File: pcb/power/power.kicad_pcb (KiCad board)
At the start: 2 copper layers, 114.3 x 74.9 mm, 27 parts, among them K1 CONN_3, P1 CONN_3X2, P2 CONN_3X2, T1 TRANSFORMER_F24-800-C2, U1 MC34063

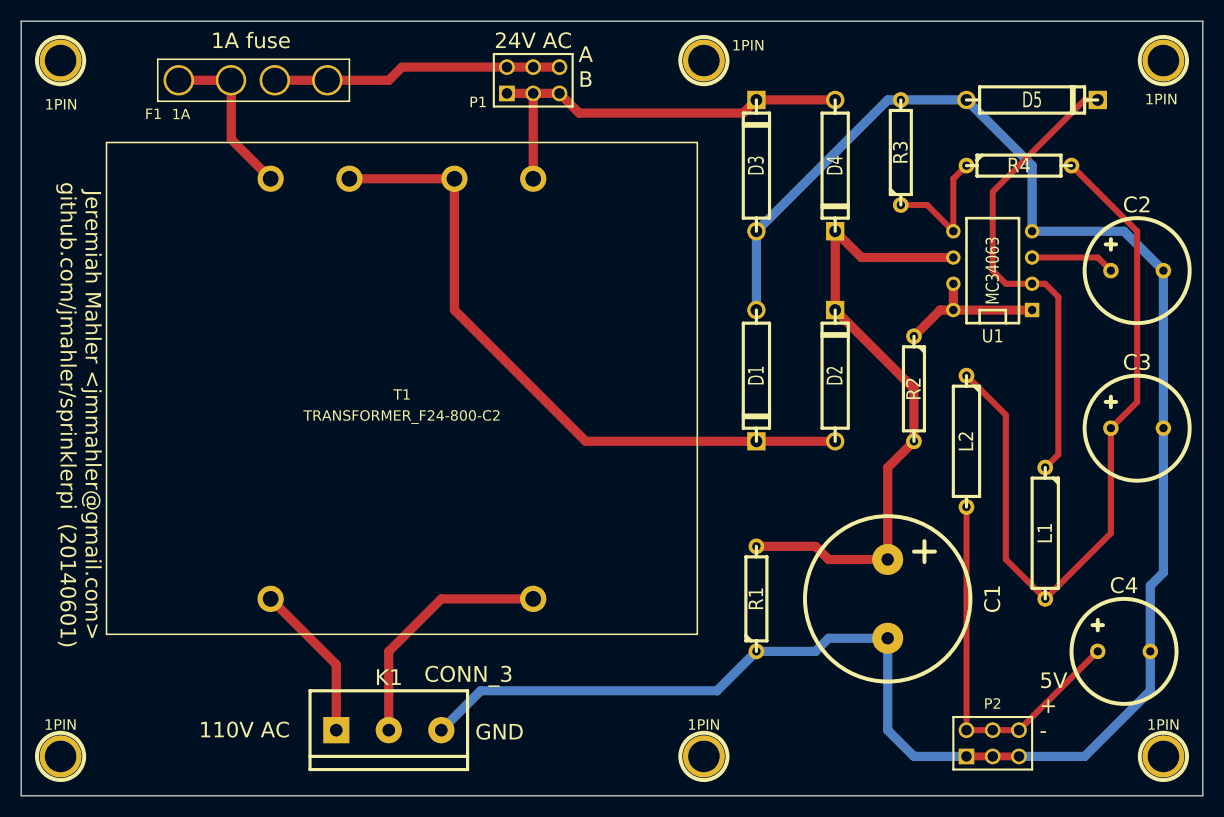
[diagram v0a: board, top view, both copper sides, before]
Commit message: proper size toroid inductor for power PCB
The power PCB has been changed to support
the proper size toroid inductor.
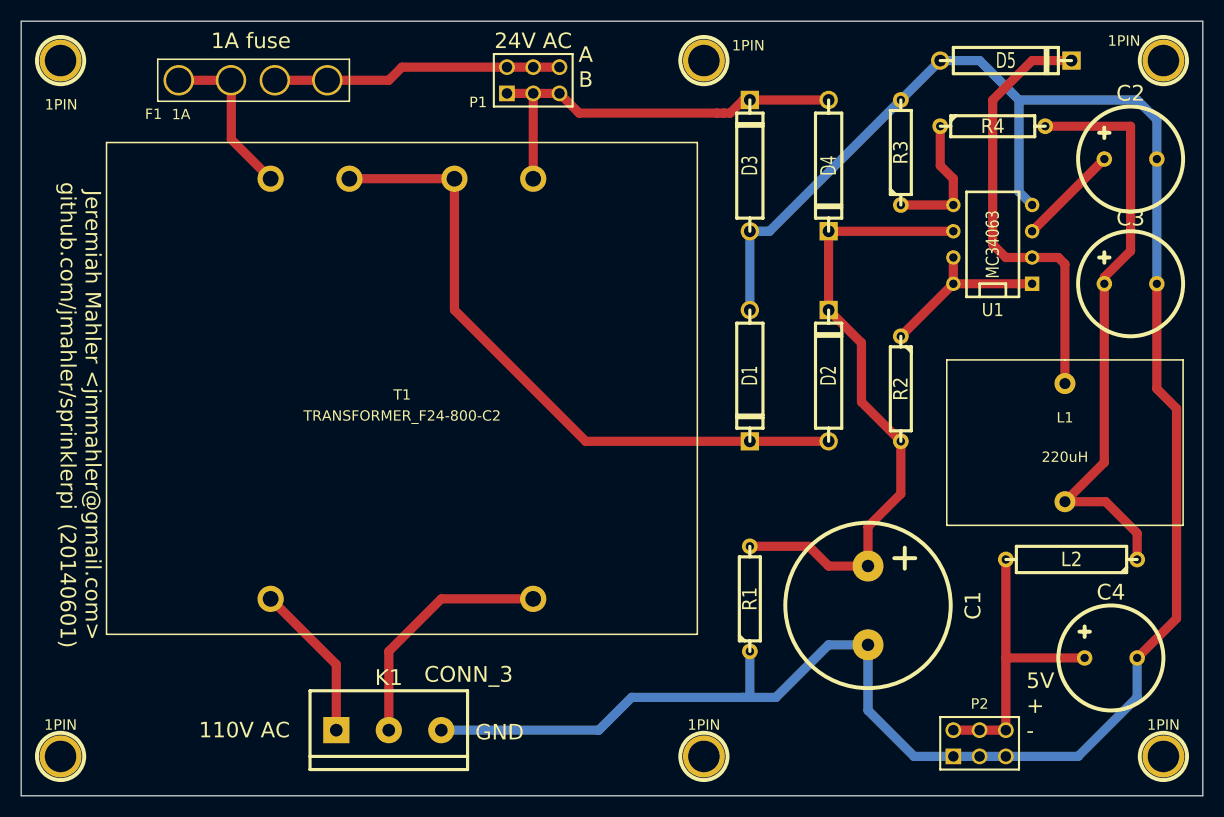
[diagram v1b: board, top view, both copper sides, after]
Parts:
- L1: footprint R5 -> INDUCTOR_TORROID_VERT_086
- moved L2 15.3 mm to (188.6, 112.4), turned to 180 degrees
- moved C3 14.0 mm to (194.3, 85.7)
- moved C2 10.8 mm to (194.3, 73.7)
- moved L1 9.09 mm to (188.0, 101.0), turned to 0 degrees
- moved R4 4.58 mm to (181.0, 70.5)
- moved D5 4.58 mm to (182.2, 64.1)
- moved U1 2.54 mm to (181.0, 81.9)
- moved C1 2.01 mm to (168.9, 116.8)
- moved C4 1.42 mm to (192.4, 121.9)
- moved P2 1.27 mm to (179.7, 130.2)
- moved R2 1.27 mm to (172.1, 95.9)
- moved D1 0.64 mm to (157.5, 94.6)
- moved D2 0.64 mm to (165.1, 94.6)
- moved D3 0.64 mm to (157.5, 74.3)
- moved D4 0.64 mm to (165.1, 74.3)
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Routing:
- net GND: track 188.8 -> 210.9 mm
- net N-0000014: track 73.0 -> 58.0 mm
- net N-000006: track 37.4 -> 29.2 mm
- net N-0000012: track 45.9 -> 42.5 mm
- net N-000009: track 15.0 -> 17.3 mm
- net N-000008: track 8.15 -> 9.88 mm
- net N-0000015: track 61.7 -> 60.9 mm
- net N-000004: track 65.0 -> 64.3 mm
- net N-0000010: track 41.3 -> 40.7 mm

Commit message: fixed power PCB name on inductor
The name on the inductor footprint is not
automatically created correctly.  It uses the
value given in the schematic when I want it to
use the part id.  Fixed by manually editing the
name.
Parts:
- L1: value 220uH -> 2116-RC
- moved L2 1.27 mm to (188.6, 113.7)
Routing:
- net N-000004: track 64.3 -> 56.9 mm
- net N-000006: track 29.2 -> 27.9 mm
- net N-000003: track 23.7 -> 22.6 mm
- net N-0000014: track 58.0 -> 57.0 mm
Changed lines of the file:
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@@
     (thickness 1.6)
     (drawings 11)
-    (tracks 103)
+    (tracks 102)
     (zones 0)
     (modules 27)
@@
     (add_net N-000009)
   )
+  (module INDUCTOR_TORROID_VERT_086 (layer F.Cu)
+    (at 187.96 100.965)
+    (descr "2 pins, inductor")
+    (tags INDUCTOR)
+    (fp_text reference L1 (at 0 -2.286) (layer F.SilkS)
+      (effects (font (size 1 1) (thickness 0.15)))
+    )
+    (fp_text value 2116-RC (at 0 1.524) (layer F.SilkS)
+      (effects (font (size 1 1) (thickness 0.15)))
+    )
+    (fp_line (start 0 -7.874) (end 11.43 -7.874) (layer F.SilkS) (width 0.15))
+    (fp_line (start 11.43 -7.874) (end 11.43 8.128) (layer F.SilkS) (width 0.15))
+    (fp_line (start 11.43 8.128) (end -11.43 8.128) (layer F.SilkS) (width 0.15))
+    (fp_line (start -11.43 8.128) (end -11.43 -7.874) (layer F.SilkS) (width 0.15))
+    (fp_line (start -11.43 -7.874) (end 0 -7.874) (layer F.SilkS) (width 0.15))
+    (pad 1 thru_hole circle (at 0 -5.588) (size 2.032 2.032) (drill 1.0668)
+      (layers *.Cu *.Mask F.SilkS)
+      (net 4 N-0000012)
+    )
+    (pad 2 thru_hole circle (at 0 5.842) (size 2.032 2.032) (drill 1.0668)
+      (layers *.Cu *.Mask F.SilkS)
+      (net 6 N-0000014)
+    )
+  )
   (module TRANSFORMER_F24-800-C2 (layer F.Cu)
     (at 123.825 75.565)
@@
     (descr "Electrolytic Capacitor, vertical, diameter 10mm, RM 5mm, Copper without +, radial,")
     (tags "Electrolytic Capacitor, vertical, diameter 10mm, RM 5mm, Elko, Electrolytkondensator, Kondensator gepolt, Durchmesser 10mm, Copper without +, radial,")
-    (fp_text reference C4 (at 0 -6.35) (layer F.SilkS)
+    (fp_text reference C4 (at -5.08 -4.445) (layer F.SilkS)
       (effects (font (size 1.524 1.524) (thickness 0.3048)))
     )
@@
     (descr "Electrolytic Capacitor, vertical, diameter 10mm, RM 5mm, Copper without +, radial,")
     (tags "Electrolytic Capacitor, vertical, diameter 10mm, RM 5mm, Elko, Electrolytkondensator, Kondensator gepolt, Durchmesser 10mm, Copper without +, radial,")
-    (fp_text reference C3 (at 0 -6.35) (layer F.SilkS)
+    (fp_text reference C3 (at -4.445 -5.08) (layer F.SilkS)
       (effects (font (size 1.524 1.524) (thickness 0.3048)))
     )
@@
     (descr "Bornier d'alimentation 3 pins")
     (tags DEV)
-    (fp_text reference K1 (at 0 -5.08) (layer F.SilkS)
+    (fp_text reference K1 (at -5.715 -5.08) (layer F.SilkS)
       (effects (font (size 1.524 1.524) (thickness 0.3048)))
     )
-    (fp_text value CONN_3 (at 7.7216 -5.3848) (layer F.SilkS)
+    (fp_text value CONN_3 (at 1.905 -5.08) (layer F.SilkS)
       (effects (font (size 1.524 1.524) (thickness 0.3048)))
     )
@@
   )
   (module R5 (layer F.Cu)
-    (at 188.595 112.395 180)
+    (at 188.595 113.665 180)
     (descr "Resistance 5 pas")
     (tags R)
@@
     )
   )
-  (module INDUCTOR_TORROID_VERT_086 (layer F.Cu)
-    (at 187.96 100.965)
-    (fp_text reference L1 (at 0 -2.286) (layer F.SilkS)
-      (effects (font (size 1 1) (thickness 0.15)))
-    )
-    (fp_text value 220uH (at 0 1.524) (layer F.SilkS)
-      (effects (font (size 1 1) (thickness 0.15)))
-    )
-    (fp_line (start 0 -7.874) (end 11.43 -7.874) (layer F.SilkS) (width 0.15))
-    (fp_line (start 11.43 -7.874) (end 11.43 8.128) (layer F.SilkS) (width 0.15))
-    (fp_line (start 11.43 8.128) (end -11.43 8.128) (layer F.SilkS) (width 0.15))
-    (fp_line (start -11.43 8.128) (end -11.43 -7.874) (layer F.SilkS) (width 0.15))
-    (fp_line (start -11.43 -7.874) (end 0 -7.874) (layer F.SilkS) (width 0.15))
-    (pad 1 thru_hole circle (at 0 -5.588) (size 2.032 2.032) (drill 1.0668)
-      (layers *.Cu *.Mask F.SilkS)
-      (net 4 N-0000012)
-    )
-    (pad 2 thru_hole circle (at 0 5.842) (size 2.032 2.032) (drill 1.0668)
-      (layers *.Cu *.Mask F.SilkS)
-      (net 6 N-0000014)
-    )
-  )
   (gr_line (start 86.995 135.255) (end 86.995 60.325) (angle 90) (layer Edge.Cuts) (width 0.1))
   (gr_line (start 201.295 135.255) (end 86.995 135.255) (angle 90) (layer Edge.Cuts) (width 0.1))
@@
     (effects (font (size 1.5 1.5) (thickness 0.3)))
   )
-  (gr_text "24V AC" (at 136.525 62.23) (layer F.SilkS)
+  (gr_text "24V AC" (at 136.525 62.0776) (layer F.SilkS)
     (effects (font (size 1.5 1.5) (thickness 0.3)))
   )
@@
     (effects (font (size 1.5 1.5) (thickness 0.3)))
   )
-  (gr_text GND (at 133.2738 129.1082) (layer F.SilkS)
+  (gr_text GND (at 133.5532 129.1336) (layer F.SilkS)
     (effects (font (size 1.5 1.5) (thickness 0.3)))
   )
@@
   (segment (start 177.165 75.565) (end 175.895 74.295) (width 0.889) (layer F.Cu) (net 5))
   (segment (start 172.085 78.105) (end 177.165 78.105) (width 0.889) (layer F.Cu) (net 5))
-  (segment (start 194.945 112.395) (end 194.945 109.855) (width 0.889) (layer F.Cu) (net 6) (status 400000))
-  (segment (start 191.897 106.807) (end 187.96 106.807) (width 0.889) (layer F.Cu) (net 6) (status 800000))
-  (segment (start 194.945 109.855) (end 191.897 106.807) (width 0.889) (layer F.Cu) (net 6))
+  (segment (start 187.96 106.807) (end 188.087 106.807) (width 0.889) (layer F.Cu) (net 6) (status C00000))
+  (segment (start 188.087 106.807) (end 194.945 113.665) (width 0.889) (layer F.Cu) (net 6) (status C00000))
   (segment (start 191.77 85.725) (end 191.77 102.997) (width 0.889) (layer F.Cu) (net 6))
   (segment (start 191.77 102.997) (end 187.96 106.807) (width 0.889) (layer F.Cu) (net 6))
@@
   (segment (start 107.315 71.755) (end 107.315 66.0654) (width 0.889) (layer F.Cu) (net 8))
   (segment (start 102.235 66.04) (end 107.2896 66.04) (width 0.889) (layer F.Cu) (net 8))
-  (segment (start 136.525 116.205) (end 127.635 116.205) (width 0.889) (layer F.Cu) (net 9))
-  (segment (start 122.555 121.285) (end 122.555 128.905) (width 0.889) (layer F.Cu) (net 9))
-  (segment (start 127.635 116.205) (end 122.555 121.285) (width 0.889) (layer F.Cu) (net 9))
+  (segment (start 122.555 128.905) (end 127.635 123.825) (width 0.889) (layer F.Cu) (net 9))
+  (segment (start 136.525 121.92) (end 136.525 116.205) (width 0.889) (layer F.Cu) (net 9))
+  (segment (start 134.62 123.825) (end 136.525 121.92) (width 0.889) (layer F.Cu) (net 9))
+  (segment (start 127.635 123.825) (end 134.62 123.825) (width 0.889) (layer F.Cu) (net 9))
+  (segment (start 128.905 75.565) (end 154.305 100.965) (width 0.889) (layer F.Cu) (net 10))
+  (segment (start 154.305 100.965) (end 157.48 100.965) (width 0.889) (layer F.Cu) (net 10))
   (segment (start 157.48 100.965) (end 165.1 100.965) (width 0.889) (layer F.Cu) (net 10))
-  (segment (start 128.905 75.565) (end 128.905 88.265) (width 0.889) (layer F.Cu) (net 10))
-  (segment (start 141.605 100.965) (end 157.48 100.965) (width 0.889) (layer F.Cu) (net 10))
-  (segment (start 128.905 88.265) (end 141.605 100.965) (width 0.889) (layer F.Cu) (net 10))
   (segment (start 118.745 75.565) (end 128.905 75.565) (width 0.889) (layer F.Cu) (net 10))
-  (segment (start 111.125 116.205) (end 117.475 122.555) (width 0.889) (layer F.Cu) (net 11))
-  (segment (start 117.475 122.555) (end 117.475 128.905) (width 0.889) (layer F.Cu) (net 11))
+  (segment (start 117.475 128.905) (end 111.125 122.555) (width 0.889) (layer F.Cu) (net 11))
+  (segment (start 111.125 122.555) (end 111.125 116.205) (width 0.889) (layer F.Cu) (net 11))
+  (segment (start 182.245 113.665) (end 182.245 121.92) (width 0.889) (layer F.Cu) (net 12) (status 400000))
   (segment (start 189.865 121.92) (end 182.245 121.92) (width 0.889) (layer F.Cu) (net 12))
-  (segment (start 182.245 112.395) (end 182.245 121.92) (width 0.889) (layer F.Cu) (net 12))
   (segment (start 182.245 121.92) (end 182.245 128.905) (width 0.889) (layer F.Cu) (net 12))
   (segment (start 179.705 128.905) (end 182.245 128.905) (width 0.889) (layer F.Cu) (net 12))

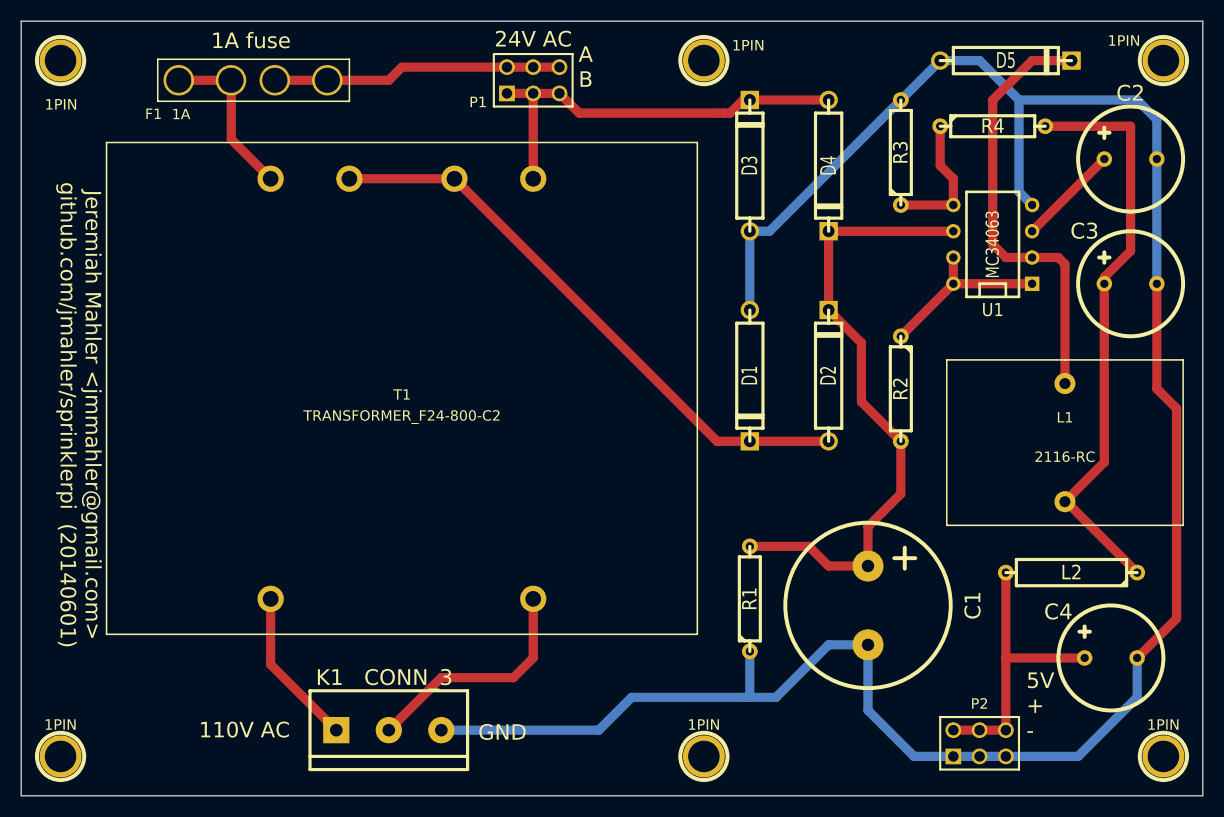
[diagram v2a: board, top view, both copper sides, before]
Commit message: fixed minor power PCB problems
Fixed several issues with the power PCB.

  - fuse holder
    - increased inner diameter to fix tight fit
    - increased outer diameter to increase pad surface
  - switched terminal connector with larger hole size
    - 1.25 -> 1.54 mm
  - fixed size for C2 and C4 capacitors

Added a bill of materials that can be uploaded to Digi-Key
or anywhere else to get a listing of parts.
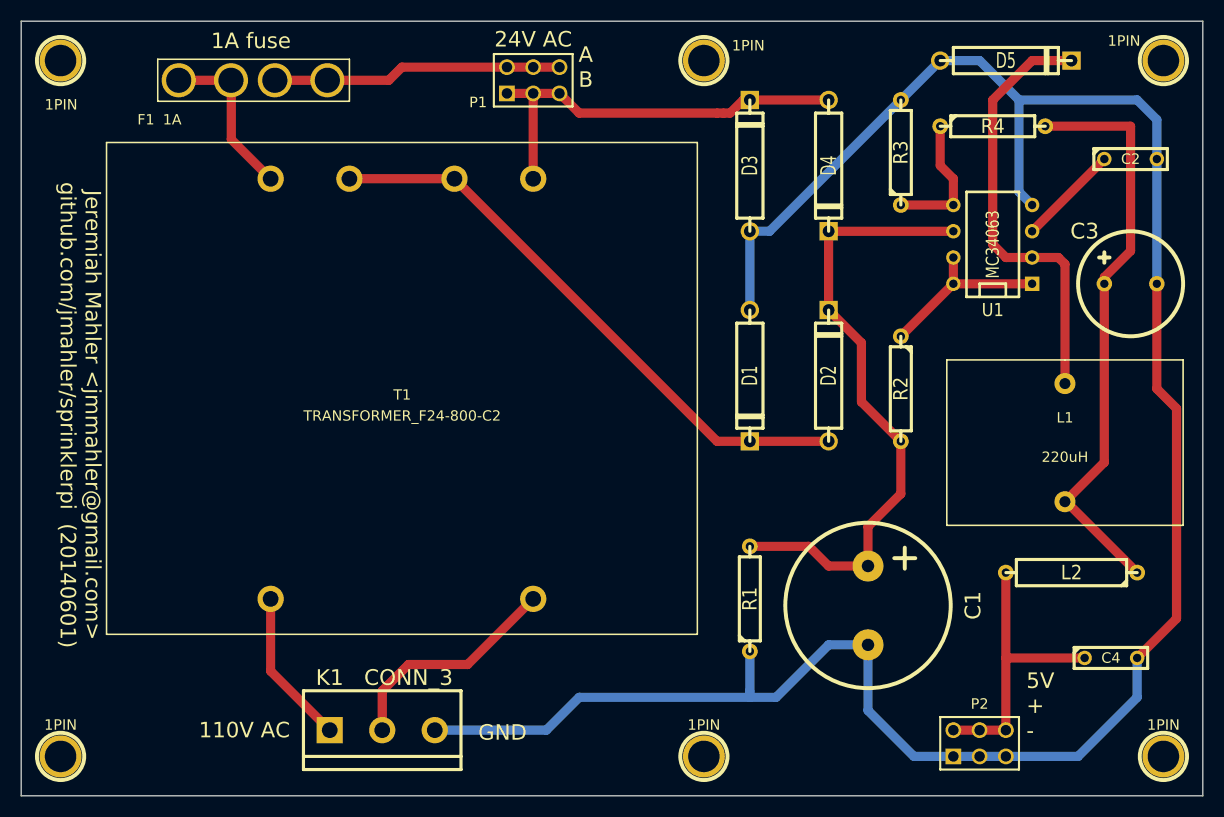
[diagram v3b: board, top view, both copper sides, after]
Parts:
- C2, C4: footprint Elko_vert_DM10_RM5_CopperClear -> C2
- K1: footprint bornier3_V -> bornier3
- L1: value 2116-RC -> 220uH
- moved K1 0.64 mm to (121.9, 128.9)
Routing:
- net GND: track 210.9 -> 211.5 mm

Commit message: power PCB, expanded 5V to 4-pin
Previously the 5V output header was
three pairs of pins.  But this would only
support two control boards and one PI.
It has been expanded to four to support
three control boards and one PI.
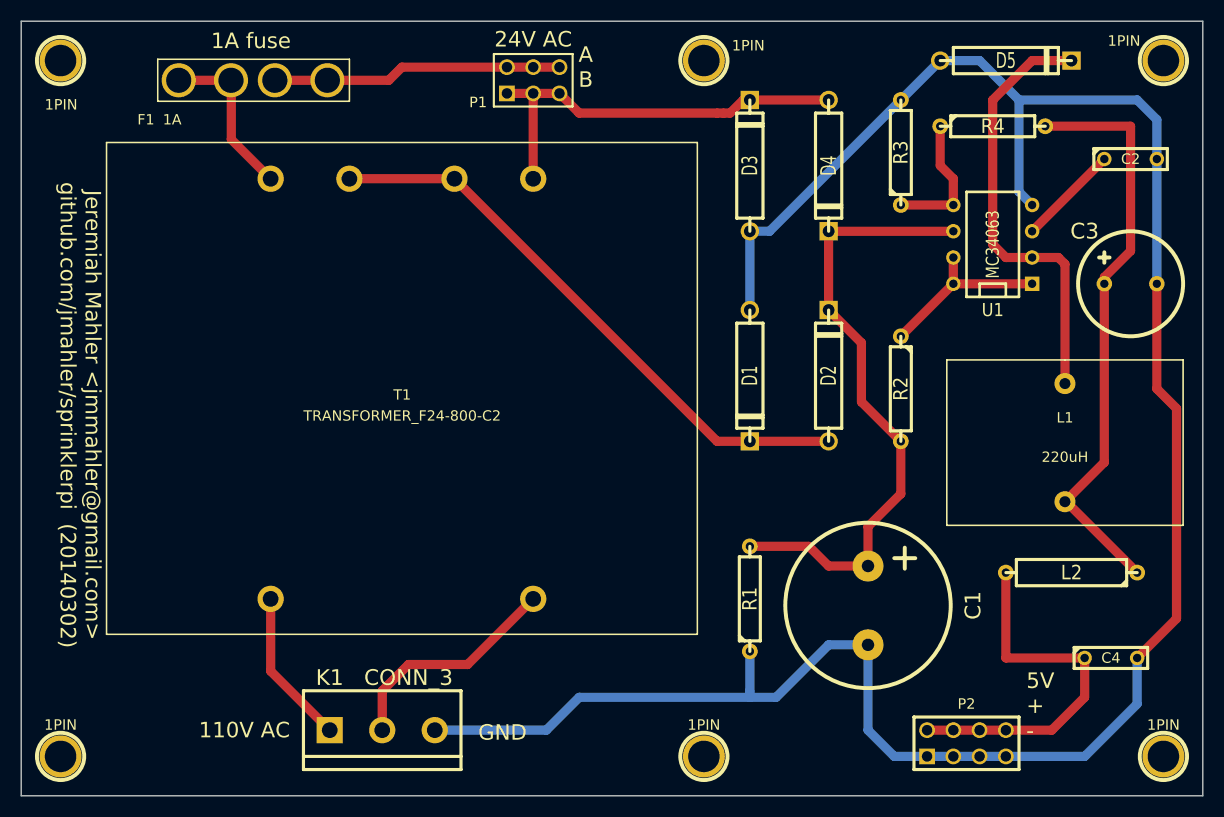
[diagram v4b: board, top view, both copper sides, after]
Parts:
- P2: value CONN_3X2 -> CONN_4X2; footprint pin_array_3x2 -> pin_array_4x2
- moved P2 1.27 mm to (178.4, 130.2)
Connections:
- C4 pad 1: N-000006 (its old number) -> N-000005
- L2 pad 2: N-000006 (its old number) -> N-000005
- P2 pad 2: N-000006 (its old number) -> N-000005
- P2 pad 4: N-000006 (its old number) -> N-000005
- P2 pad 6: N-000006 (its old number) -> N-000005
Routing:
- net N-000005: track 0.00 -> 36.2 mm
- net N-000006 (its old number): track 27.9 -> 0.00 mm
- net GND: track 211.5 -> 213.0 mm
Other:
- board text added: "Jeremiah Mahler <jmmahler@gmail.com> github.com/jmahler/sprinklerpi (20140302)"
- board text removed: "Jeremiah Mahler <jmmahler@gmail.com> github.com/jmahler/sprinklerpi (20140601)"
